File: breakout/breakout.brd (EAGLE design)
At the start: 485 x 130 mm, 239 parts, among them J17 1789074, J26 69168-124HLF, J29 SJ1-3514-SMT-TR, J31 69168-116HLF, J32 12226-8250-00FR, J33 1888276, J34 69168-116HLF, J35 1888276, Q1 SI1012R, Q2 SI1012R, Q3 SI1012R, Q4 SI1012R, Q5 SI1012R, Q6 SI1012R, Q7 SI1012R, Q8 SI1012R, U1 SK6805-E-J, U10 TXB0101, U11 SK6805-E-J, U12 SK6805-E-J, U13 SK6805-E-J, U14 SK6805-E-J, U15 SK6805-E-J, U16 SK6805-E-J, U17 SK6805-E-J, U18 SK6805-E-J, U19 SK6805-E-J, U2 SK6805-E-J, U20 SK6805-E-J, U21 SK6805-E-J, U22 SK6805-E-J, U23 SK6805-E-J, U24 SK6805-E-J, U25 SK6805-E-J, U26 SK6805-E-J, U27 SK6805-E-J, U28 SK6805-E-J, U29 SK6805-E-J, U3 SK6805-E-J, U30 SK6805-E-J, U31 SK6805-E-J, U32 SK6805-E-J, U33 SK6805-E-J, U34 SK6805-E-J, U35 SK6805-E-J, U36 SK6805-E-J, U37 SK6805-E-J, U38 SK6805-E-J, U39 SK6805-E-J, U4 SK6805-E-J, U40 SK6805-E-J, U41 SK6805-E-J, U42 SK6805-E-J, U43 G6K-2F-RF, U44 G6K-2F-RF, U45 G6K-2F-RF, U46 G6K-2F-RF, U47 LTM4622A, U48 SI8610, U49 TINY-FPGA-BX, U5 SK6805-E-J, U50 TCA9555, U51 FIN1032MTCX, U52 SN65LVDS9638DGN, U53 SN65LVDS9638DGN, U6 SK6805-E-J, U7 SK6805-E-J, U8 SK6805-E-J, U9 SK6805-E-J

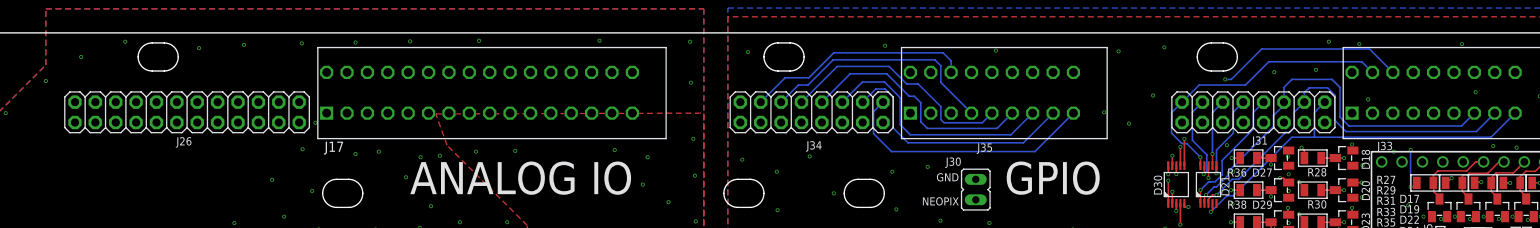
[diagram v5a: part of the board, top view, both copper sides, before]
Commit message: Increased space between IDC headers and wire terminals on breakout
- Moved by 2mm so that an IDC connector can actually plug into the
header.
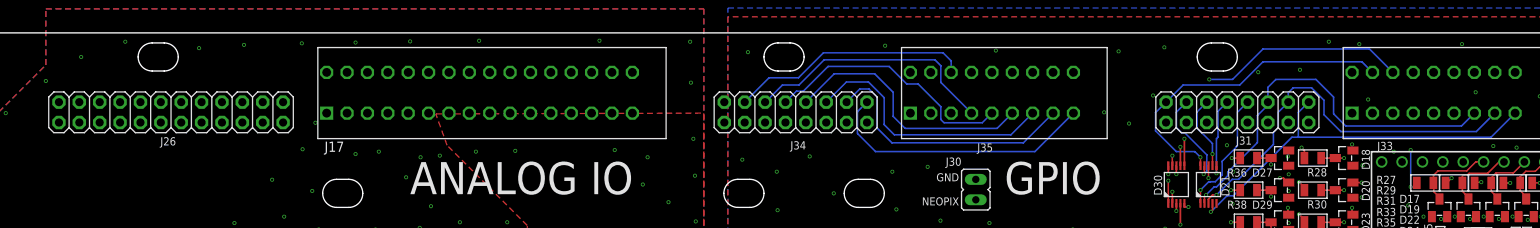
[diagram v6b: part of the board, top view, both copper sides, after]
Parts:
- moved J26 2.00 mm to (298.6, 120.0)
- moved J31 2.00 mm to (431.5, 120.0)
- moved J34 2.00 mm to (376.4, 120.0)
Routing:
- net DOUT0: track 49.2 -> 53.0 mm
- net DOUT1: track 52.7 -> 55.7 mm
- net DOUT2: track 49.4 -> 52.2 mm
- net DIN4: track 64.2 -> 66.5 mm
- net DIN3: track 77.5 -> 79.5 mm
- net DIN0: track 76.1 -> 78.1 mm
- net DIN7: track 67.3 -> 69.3 mm
- net DIN6: track 59.0 -> 61.0 mm
- net DIN5: track 70.3 -> 72.3 mm
- net DIN2: track 70.5 -> 72.5 mm
- net DIN1: track 86.4 -> 88.4 mm
- net DOUT4: track 57.7 -> 58.9 mm
- net DOUT3: track 51.2 -> 52.4 mm

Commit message: Breakout board revision 1.5
- Ready for production
- Added smd-mount folder with component positions
- As soon as I get confirmation from Filipe I will freeze this in the
revisions folder
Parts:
- added E$1, E$3, E$5: (no value), fiducial:FIDUCIAL
- moved C43 15.0 mm to (439.4, 74.9)
- moved R24 15.0 mm to (446.0, 73.4)
- moved U50 15.0 mm to (439.3, 69.9)
- moved X 15.0 mm to (47.1, 77.4)
- moved C32 15.0 mm to (325.7, 33.2)
- moved R7 15.0 mm to (327.1, 33.2)
- moved C1 15.0 mm to (452.8, 111.3)
- moved C10 15.0 mm to (346.0, 93.5)
- moved C11 15.0 mm to (307.8, 65.5)
- moved C12 15.0 mm to (307.7, 40.5)
- moved C13 15.0 mm to (307.8, 90.5)
- moved C14 15.0 mm to (307.8, 115.5)
- moved C15 15.0 mm to (243.0, 30.5)
- moved C16 15.0 mm to (203.0, 30.5)
- moved C17 15.0 mm to (163.0, 30.5)
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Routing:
- net GND: vias 1136 -> 1157
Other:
- board size 485 x 130 mm -> 505 x 160 mm
- board text added: "(262, 12)"
- board text added: "(270, 148)"
- board text added: "(473, 11)"
- board text added: "1.5"
- board text added: "Rev. 1.5 CC BY-NC-SA 4.0 JPN, JV Open Ephys 2020"
- board text added: "V-CUT"
- board text removed: "Rev. 1.5 CC BY-NC-SA 4.0 JPN, JV, MIT 2020"

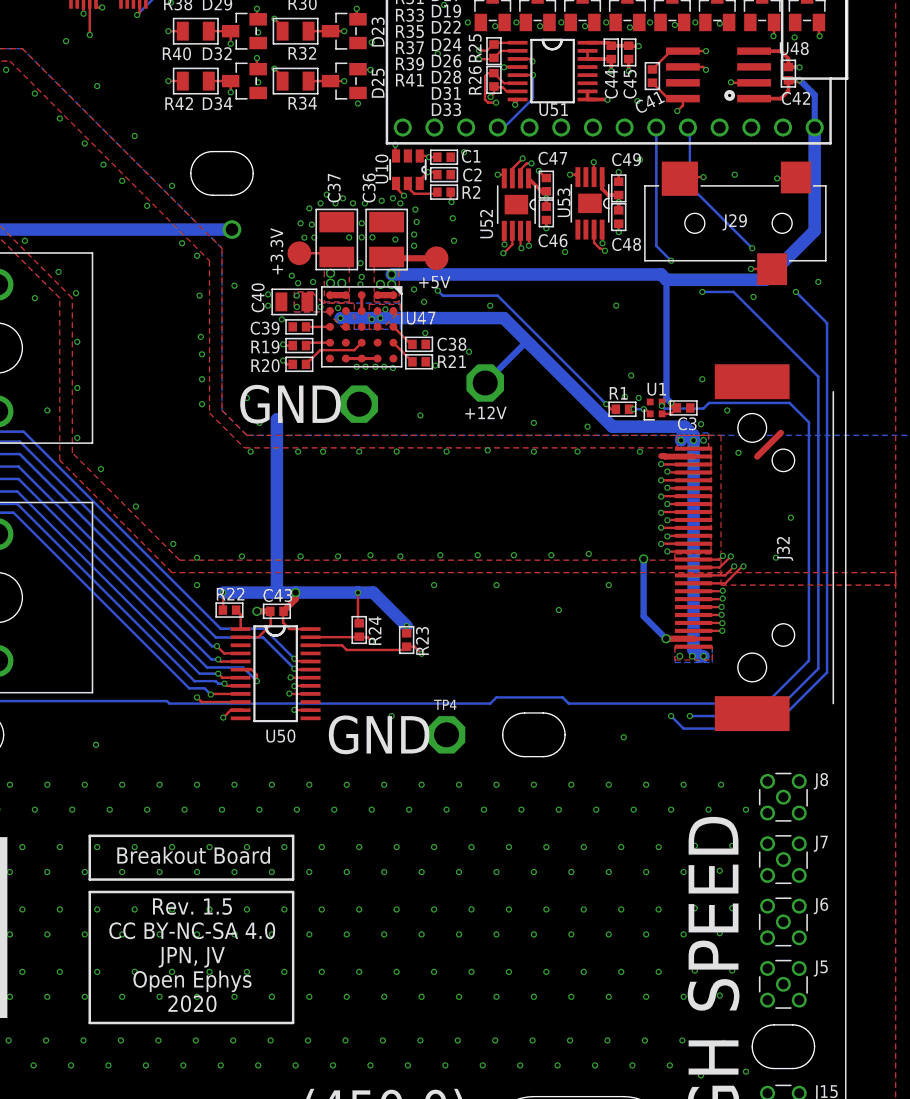
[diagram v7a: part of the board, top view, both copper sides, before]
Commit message: breakout rev. 1.6
- Minor revision that addes a load switch driven by the LM4622's PGOOD2
output between 5V and FPGA Vin. This improves the power-on behavior of
the board and prevents it from entering an unstable state that requires
a manual reset via pushing the reset button.
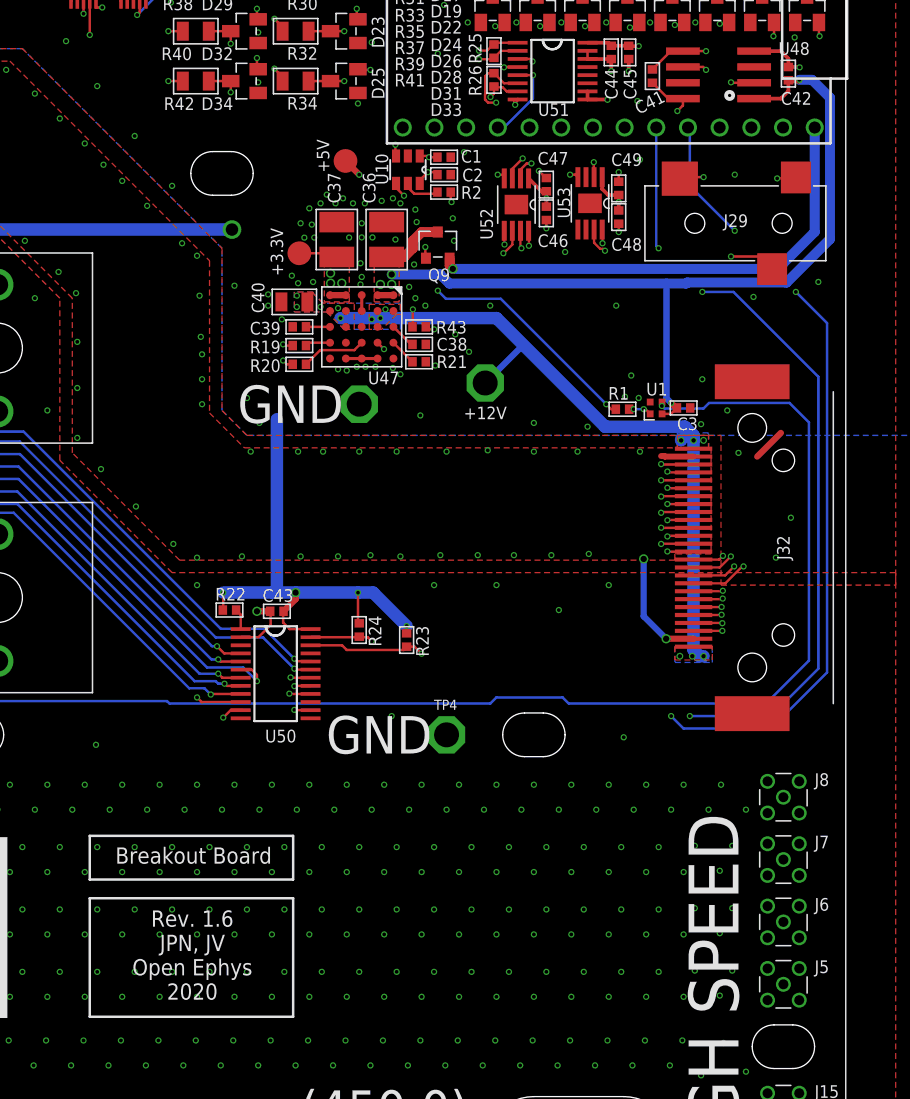
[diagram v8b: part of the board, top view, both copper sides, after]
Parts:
- added Q9: IRFML8244TRPBF, jonnew:SOT23-GSD
- added R43: 4.7k, jonnew:0402
- moved TP2 10.7 mm to (444.9, 111.0)
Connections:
- new net +5V0_GOOD: Q9.G, R43.1, U47.B4
- new net N$61: Q9.S, U49.VIN
- net +12V: now also R43.2
- net +5V0: now also Q9.D; no longer U49.VIN
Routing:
- net N$61: track 0.00 -> 39.6 mm, vias 0 -> 1
- net +5V0_GOOD: track 0.00 -> 21.8 mm, vias 0 -> 3
- net +5V0: track 1320.8 -> 1328.5 mm, vias 58 -> 59
- net +12V: track 55.4 -> 60.1 mm, vias 14 -> 15
- net GND: vias 1157 -> 1159
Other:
- board text added: "Rev. 1.6 JPN, JV Open Ephys 2020"
- board text removed: "Rev. 1.5 CC BY-NC-SA 4.0 JPN, JV Open Ephys 2020"
